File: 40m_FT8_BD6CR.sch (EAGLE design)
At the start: 54 parts, among them IC1 LM7805, IC2 NE602, Q1 2N3904, Q2 2N3904, Q3 2N3904, Q4 BD139, Q5 7074, Q6 7074, X1 JST-XH-02-PIN, X2 JST-XH-02-PIN, X3 JST-XH-02-PIN

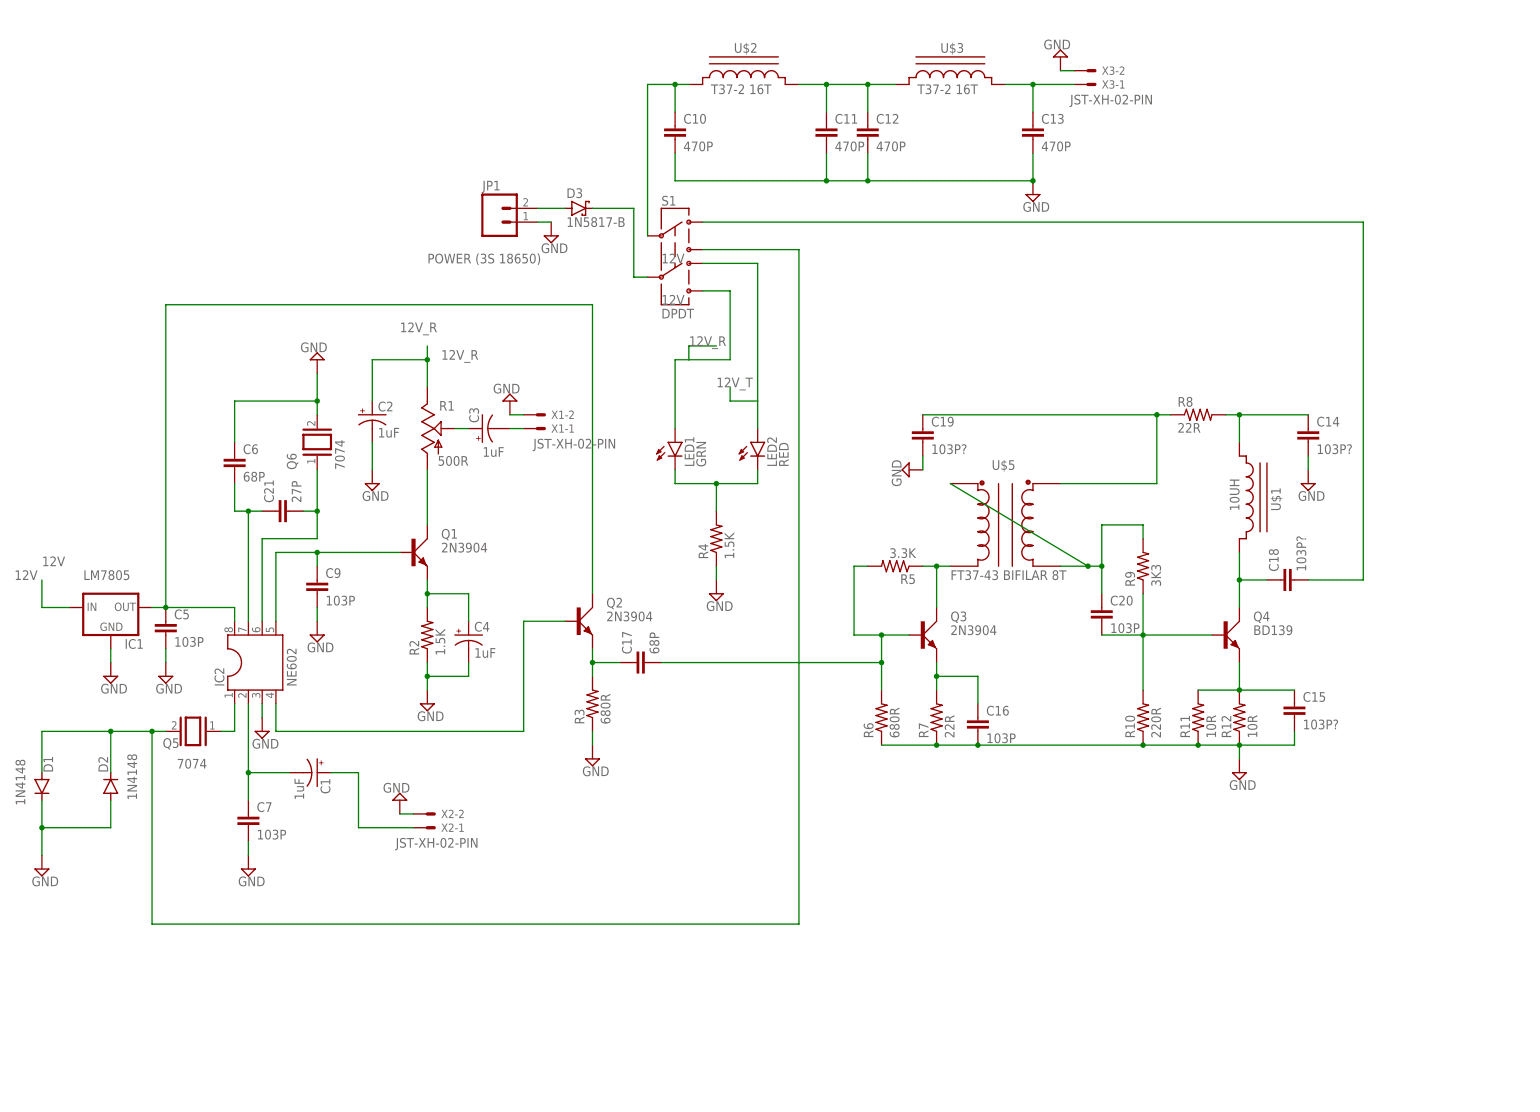
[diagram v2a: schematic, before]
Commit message: updated with vias.
Still some work to do on vias and routing
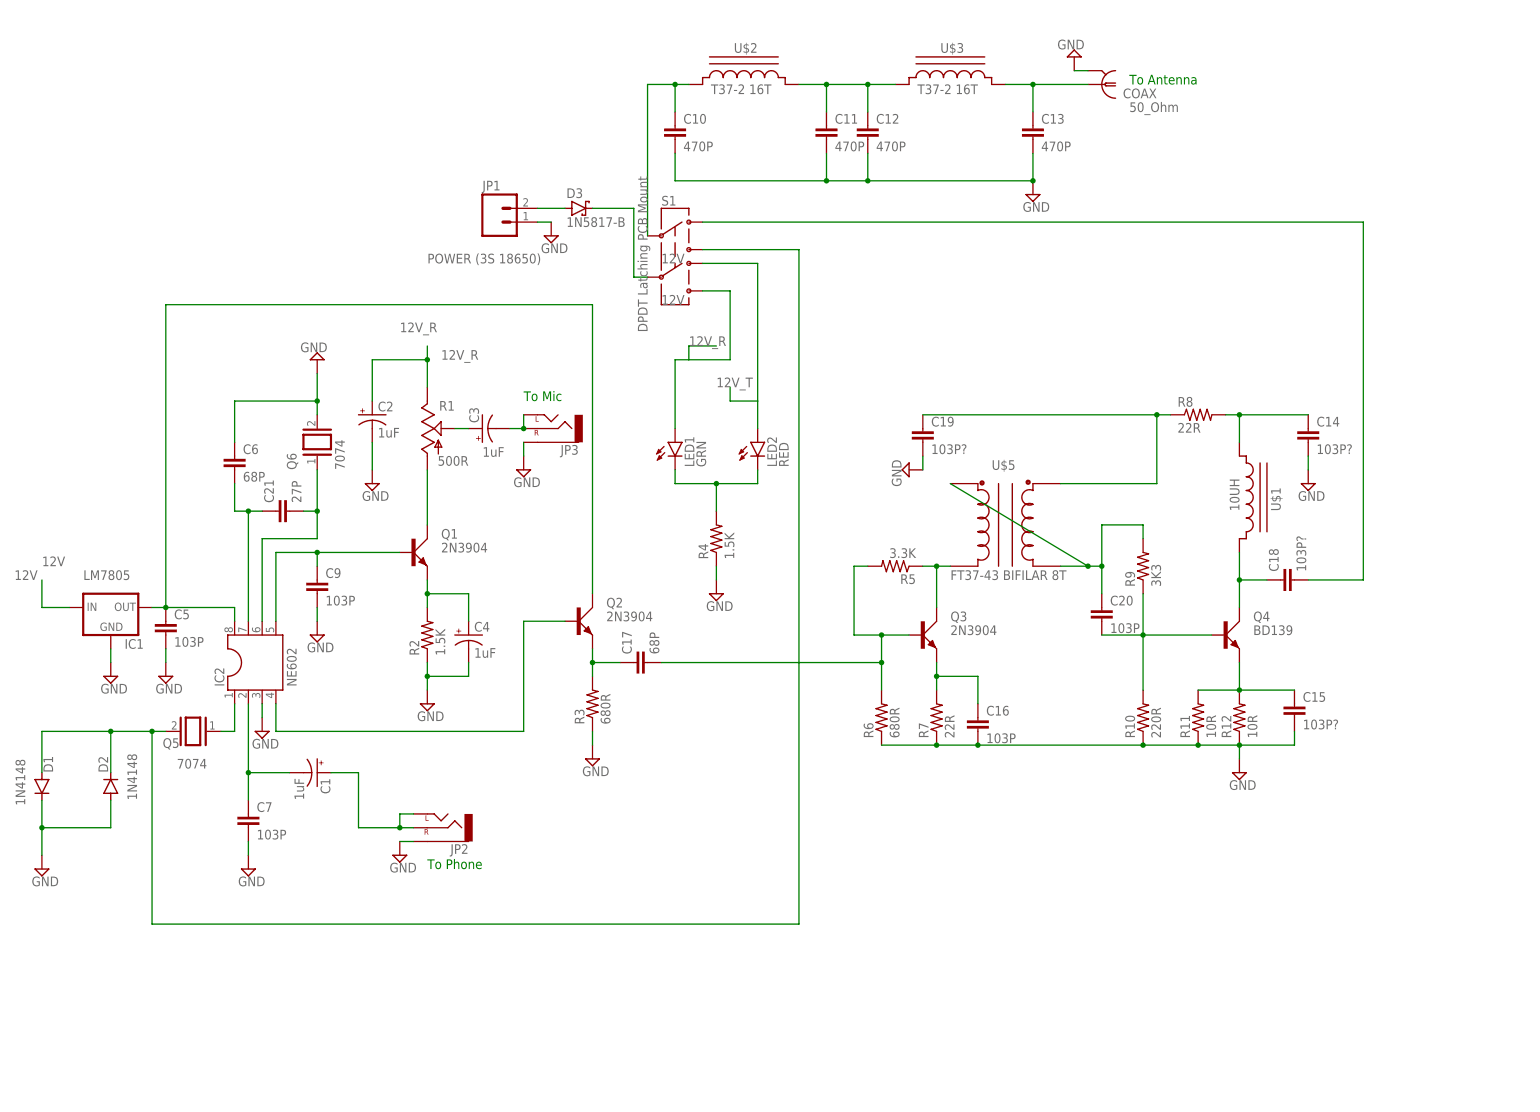
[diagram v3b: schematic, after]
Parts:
- removed X1, X2, X3: JST-XH-02-PIN, Rembrandt Electronics - JST XH Connectors v1-0:JST-XH-02-PIN-LONG-PAD
- added COAX: 50_Ohm, con-coax:R141426
- added JP2, JP3: (no value), SparkFun-Connectors:AUDIO-JACKPTH
- S1: value DPDT -> DPDT Latching PCB Mount
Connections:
- net GND: now also COAX.2, JP2.SLEEVE, JP3.SLEEVE; no longer X1-2.S, X2-2.S, X3-2.S
- net N$27: now also JP2.LEFT, JP2.RIGHT; no longer X2-1.S
- net N$3: now also COAX.1; no longer X3-1.S
- net N$7: now also JP3.LEFT, JP3.RIGHT; no longer X1-1.S
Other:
- note added: "To Antenna"
- note added: "To Mic"
- note added: "To Phone"
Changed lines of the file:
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@@
 <part name="C16" library="rcl" library_urn="urn:adsk.eagle:library:334" deviceset="C-EU" device="050-025X075" package3d_urn="urn:adsk.eagle:package:23637/1" value="103P"/>
 <part name="C17" library="rcl" library_urn="urn:adsk.eagle:library:334" deviceset="C-EU" device="050-025X075" package3d_urn="urn:adsk.eagle:package:23637/1" value="68P"/>
-<part name="S1" library="SparkFun-Electromechanical" library_urn="urn:adsk.eagle:library:516" deviceset="SWITCH-DPDT" device="AYZ0202" value="DPDT"/>
+<part name="S1" library="SparkFun-Electromechanical" library_urn="urn:adsk.eagle:library:516" deviceset="SWITCH-DPDT" device="AYZ0202" value="DPDT Latching PCB Mount"/>
 <part name="SUPPLY2" library="supply2" library_urn="urn:adsk.eagle:library:372" deviceset="GND" device=""/>
 <part name="SUPPLY3" library="supply2" library_urn="urn:adsk.eagle:library:372" deviceset="GND" device=""/>
@@
 <part name="SUPPLY19" library="supply2" library_urn="urn:adsk.eagle:library:372" deviceset="GND" device=""/>
 <part name="SUPPLY20" library="supply2" library_urn="urn:adsk.eagle:library:372" deviceset="GND" device=""/>
-<part name="X1" library="Rembrandt Electronics - JST XH Connectors v1-0" deviceset="JST-XH-02-PIN" device="-LONG-PAD" value="JST-XH-02-PIN"/>
-<part name="X2" library="Rembrandt Electronics - JST XH Connectors v1-0" deviceset="JST-XH-02-PIN" device="-LONG-PAD" value="JST-XH-02-PIN"/>
-<part name="X3" library="Rembrandt Electronics - JST XH Connectors v1-0" deviceset="JST-XH-02-PIN" device="-LONG-PAD" value="JST-XH-02-PIN"/>
 <part name="R2" library="rcl" library_urn="urn:adsk.eagle:library:334" deviceset="R-US_" device="0207/10" package3d_urn="urn:adsk.eagle:package:23491/2" value="1.5K"/>
 <part name="R3" library="rcl" library_urn="urn:adsk.eagle:library:334" deviceset="R-US_" device="0207/10" package3d_urn="urn:adsk.eagle:package:23491/2" value="680R"/>
@@
 <part name="R11" library="rcl" library_urn="urn:adsk.eagle:library:334" deviceset="R-US_" device="0207/10" package3d_urn="urn:adsk.eagle:package:23491/2" value="10R"/>
 <part name="R12" library="rcl" library_urn="urn:adsk.eagle:library:334" deviceset="R-US_" device="0207/10" package3d_urn="urn:adsk.eagle:package:23491/2" value="10R"/>
+<part name="JP2" library="SparkFun-Connectors" deviceset="AUDIO-JACK" device="PTH"/>
+<part name="JP3" library="SparkFun-Connectors" deviceset="AUDIO-JACK" device="PTH"/>
+<part name="COAX" library="con-coax" library_urn="urn:adsk.eagle:library:133" deviceset="R141426" device="" package3d_urn="urn:adsk.eagle:package:6203/1" value="50_Ohm"/>
 </parts>
 <sheets>
 <sheet>
 <plain>
+<text x="81.28" y="17.78" size="1.778" layer="91">To Phone</text>
+<text x="210.82" y="162.56" size="1.778" layer="91">To Antenna</text>
+<text x="99.06" y="104.14" size="1.778" layer="91">To Mic</text>
 </plain>
 <instances>
@@
 <instance part="S1" gate="G$1" x="127" y="132.08" smashed="yes">
 <attribute name="NAME" x="124.46" y="140.208" size="1.778" layer="95"/>
-<attribute name="VALUE" x="124.46" y="119.38" size="1.778" layer="96"/>
+<attribute name="VALUE" x="121.92" y="116.84" size="1.778" layer="96" rot="R90"/>
 </instance>
 <instance part="SUPPLY2" gate="GND" x="104.14" y="134.62" smashed="yes">
@@
 <attribute name="VALUE" x="191.135" y="139.065" size="1.778" layer="96"/>
 </instance>
-<instance part="SUPPLY5" gate="GND" x="198.12" y="167.64" smashed="yes" rot="R180">
-<attribute name="VALUE" x="200.025" y="170.815" size="1.778" layer="96" rot="R180"/>
+<instance part="SUPPLY5" gate="GND" x="200.66" y="167.64" smashed="yes" rot="R180">
+<attribute name="VALUE" x="202.565" y="170.815" size="1.778" layer="96" rot="R180"/>
 </instance>
 <instance part="SUPPLY6" gate="GND" x="134.62" y="68.58" smashed="yes">
@@
 <attribute name="VALUE" x="241.935" y="85.725" size="1.778" layer="96"/>
 </instance>
-<instance part="SUPPLY9" gate="GND" x="76.2" y="30.48" smashed="yes" rot="R180">
-<attribute name="VALUE" x="78.105" y="33.655" size="1.778" layer="96" rot="R180"/>
+<instance part="SUPPLY9" gate="GND" x="76.2" y="20.32" smashed="yes">
+<attribute name="VALUE" x="74.295" y="17.145" size="1.778" layer="96"/>
 </instance>
 <instance part="C18" gate="G$1" x="238.76" y="71.12" smashed="yes" rot="R90">
@@
 <attribute name="VALUE" x="46.355" y="14.605" size="1.778" layer="96"/>
 </instance>
-<instance part="SUPPLY15" gate="GND" x="96.52" y="104.14" smashed="yes" rot="R180">
-<attribute name="VALUE" x="98.425" y="107.315" size="1.778" layer="96" rot="R180"/>
+<instance part="SUPPLY15" gate="GND" x="99.06" y="91.44" smashed="yes">
+<attribute name="VALUE" x="97.155" y="88.265" size="1.778" layer="96"/>
 </instance>
 <instance part="SUPPLY16" gate="GND" x="60.96" y="60.96" smashed="yes">
@@
 <attribute name="VALUE" x="79.375" y="45.085" size="1.778" layer="96"/>
 </instance>
-<instance part="X1" gate="-2" x="101.6" y="101.6" smashed="yes">
-<attribute name="NAME" x="104.14" y="100.838" size="1.524" layer="95"/>
-</instance>
-<instance part="X1" gate="-1" x="101.6" y="99.06" smashed="yes">
-<attribute name="NAME" x="104.14" y="98.298" size="1.524" layer="95"/>
-<attribute name="VALUE" x="100.838" y="95.377" size="1.778" layer="96"/>
-</instance>
-<instance part="X2" gate="-2" x="81.28" y="27.94" smashed="yes">
-<attribute name="NAME" x="83.82" y="27.178" size="1.524" layer="95"/>
-</instance>
-<instance part="X2" gate="-1" x="81.28" y="25.4" smashed="yes">
-<attribute name="NAME" x="83.82" y="24.638" size="1.524" layer="95"/>
-<attribute name="VALUE" x="75.438" y="21.717" size="1.778" layer="96"/>
-</instance>
-<instance part="X3" gate="-2" x="203.2" y="165.1" smashed="yes">
-<attribute name="NAME" x="205.74" y="164.338" size="1.524" layer="95"/>
-</instance>
-<instance part="X3" gate="-1" x="203.2" y="162.56" smashed="yes">
-<attribute name="NAME" x="205.74" y="161.798" size="1.524" layer="95"/>
-<attribute name="VALUE" x="199.898" y="158.877" size="1.778" layer="96"/>
-</instance>
 <instance part="R2" gate="G$1" x="81.28" y="60.96" smashed="yes" rot="R90">
 <attribute name="NAME" x="79.7814" y="57.15" size="1.778" layer="95" rot="R90"/>
@@
 <attribute name="NAME" x="229.6414" y="41.91" size="1.778" layer="95" rot="R90"/>
 <attribute name="VALUE" x="234.442" y="41.91" size="1.778" layer="96" rot="R90"/>
+</instance>
+<instance part="JP2" gate="G$1" x="83.82" y="25.4" smashed="yes" rot="R180">
+<attribute name="NAME" x="88.9" y="22.352" size="1.778" layer="95" rot="R180"/>
+<attribute name="VALUE" x="88.9" y="30.48" size="1.778" layer="96" rot="R180"/>
+</instance>
+<instance part="JP3" gate="G$1" x="104.14" y="99.06" smashed="yes" rot="R180">
+<attribute name="NAME" x="109.22" y="96.012" size="1.778" layer="95" rot="R180"/>
+<attribute name="VALUE" x="109.22" y="104.14" size="1.778" layer="96" rot="R180"/>
+</instance>
+<instance part="COAX" gate="G$1" x="205.74" y="162.56" smashed="yes" rot="R180">
+<attribute name="VALUE" x="210.82" y="157.48" size="1.778" layer="96"/>
+<attribute name="NAME" x="215.9" y="161.798" size="1.778" layer="95" rot="R180"/>
 </instance>
 </instances>
@@
 <segment>
 <pinref part="SUPPLY5" gate="GND" pin="GND"/>
-<wire x1="200.66" y1="165.1" x2="198.12" y2="165.1" width="0.1524" layer="91"/>
-<pinref part="X3" gate="-2" pin="S"/>
+<wire x1="200.66" y1="165.1" x2="203.2" y2="165.1" width="0.1524" layer="91"/>
+<pinref part="COAX" gate="G$1" pin="2"/>
 </segment>
 <segment>
@@
 <segment>
 <pinref part="SUPPLY9" gate="GND" pin="GND"/>
-<wire x1="78.74" y1="27.94" x2="76.2" y2="27.94" width="0.1524" layer="91"/>
-<pinref part="X2" gate="-2" pin="S"/>
+<wire x1="78.74" y1="22.86" x2="76.2" y2="22.86" width="0.1524" layer="91"/>
+<pinref part="JP2" gate="G$1" pin="SLEEVE"/>
 </segment>
 <segment>
@@
 </segment>
 <segment>
-<pinref part="X1" gate="-2" pin="S"/>
 <pinref part="SUPPLY15" gate="GND" pin="GND"/>
-<wire x1="99.06" y1="101.6" x2="96.52" y2="101.6" width="0.1524" layer="91"/>
+<wire x1="99.06" y1="96.52" x2="99.06" y2="93.98" width="0.1524" layer="91"/>
+<pinref part="JP3" gate="G$1" pin="SLEEVE"/>
 </segment>
 <segment>
@@
 <segment>
 <pinref part="U$3" gate="G$1" pin="CA"/>
-<wire x1="200.66" y1="162.56" x2="193.04" y2="162.56" width="0.1524" layer="91"/>
 <pinref part="C13" gate="G$1" pin="1"/>
+<wire x1="203.2" y1="162.56" x2="193.04" y2="162.56" width="0.1524" layer="91"/>
 <wire x1="193.04" y1="162.56" x2="187.96" y2="162.56" width="0.1524" layer="91"/>
 <wire x1="193.04" y1="157.48" x2="193.04" y2="162.56" width="0.1524" layer="91"/>
 <junction x="193.04" y="162.56"/>
-<pinref part="X3" gate="-1" pin="S"/>
+<pinref part="COAX" gate="G$1" pin="1"/>
 </segment>
 </net>
@@
 <net name="N$27" class="0">
 <segment>
-<wire x1="78.74" y1="25.4" x2="68.58" y2="25.4" width="0.1524" layer="91"/>
+<wire x1="78.74" y1="25.4" x2="76.2" y2="25.4" width="0.1524" layer="91"/>
+<wire x1="76.2" y1="25.4" x2="68.58" y2="25.4" width="0.1524" layer="91"/>
 <wire x1="68.58" y1="25.4" x2="68.58" y2="35.56" width="0.1524" layer="91"/>
 <pinref part="C1" gate="G$1" pin="+"/>
 <wire x1="68.58" y1="35.56" x2="63.5" y2="35.56" width="0.1524" layer="91"/>
-<pinref part="X2" gate="-1" pin="S"/>
+<pinref part="JP2" gate="G$1" pin="RIGHT"/>
+<pinref part="JP2" gate="G$1" pin="LEFT"/>
+<wire x1="78.74" y1="27.94" x2="76.2" y2="27.94" width="0.1524" layer="91"/>
+<wire x1="76.2" y1="27.94" x2="76.2" y2="25.4" width="0.1524" layer="91"/>
+<junction x="76.2" y="25.4"/>
 </segment>
 </net>
@@
 <net name="N$7" class="0">
 <segment>
-<pinref part="X1" gate="-1" pin="S"/>
 <pinref part="C3" gate="G$1" pin="-"/>
 <wire x1="99.06" y1="99.06" x2="96.52" y2="99.06" width="0.1524" layer="91"/>
-</segment>
-</net>
+<pinref part="JP3" gate="G$1" pin="RIGHT"/>
+<pinref part="JP3" gate="G$1" pin="LEFT"/>
+<wire x1="99.06" y1="99.06" x2="99.06" y2="101.6" width="0.1524" layer="91"/>
+<junction x="99.06" y="99.06"/>
+</segment>
+</net>
